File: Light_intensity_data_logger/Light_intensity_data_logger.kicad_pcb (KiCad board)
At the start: 2 copper layers, 105 x 69 mm, 27 parts, among them J1 Wire_to_Vbat, Q1 NTJD4001NT1G, Q2 NTJD4001NT1G, U1 BME280, U2 TCS34725FN, U3 TSL25911FN, U4 Teensy3.6

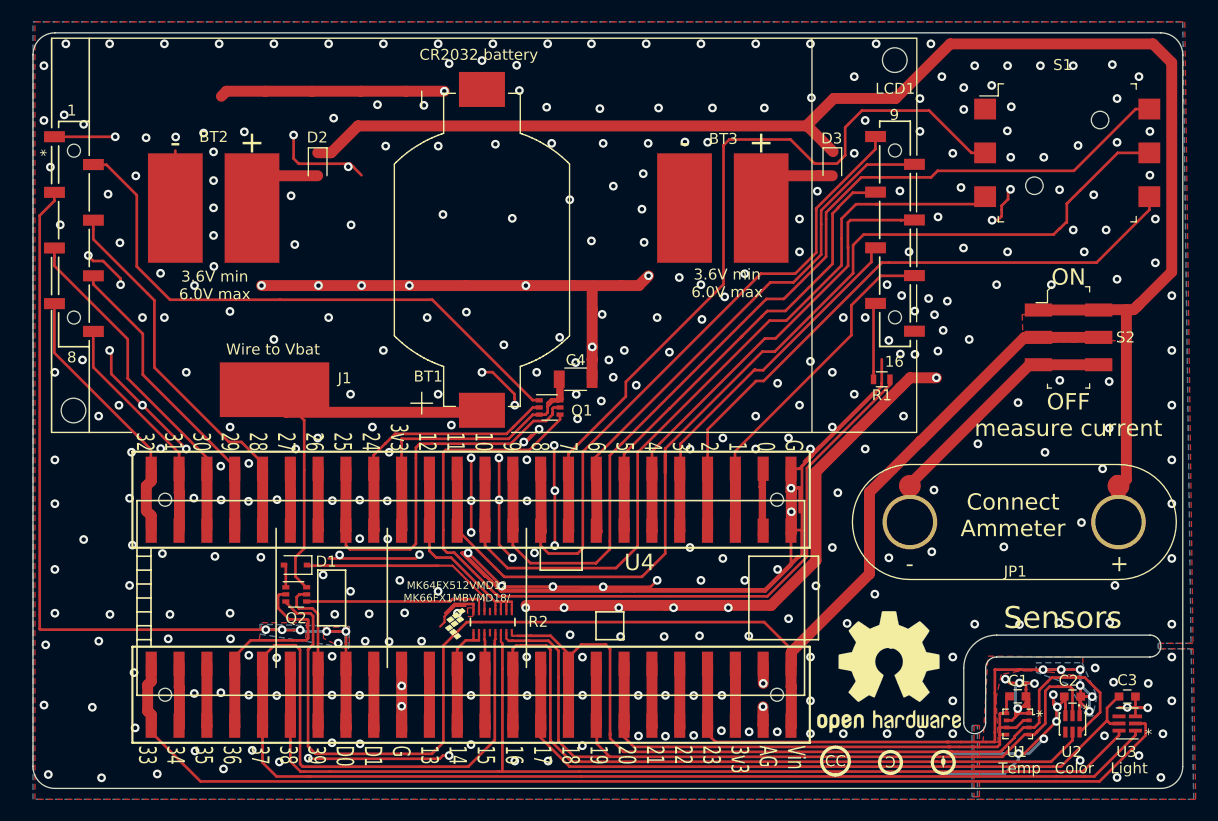
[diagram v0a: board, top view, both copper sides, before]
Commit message: Parts numbered in order, courtyards fixed, bigger banana pads
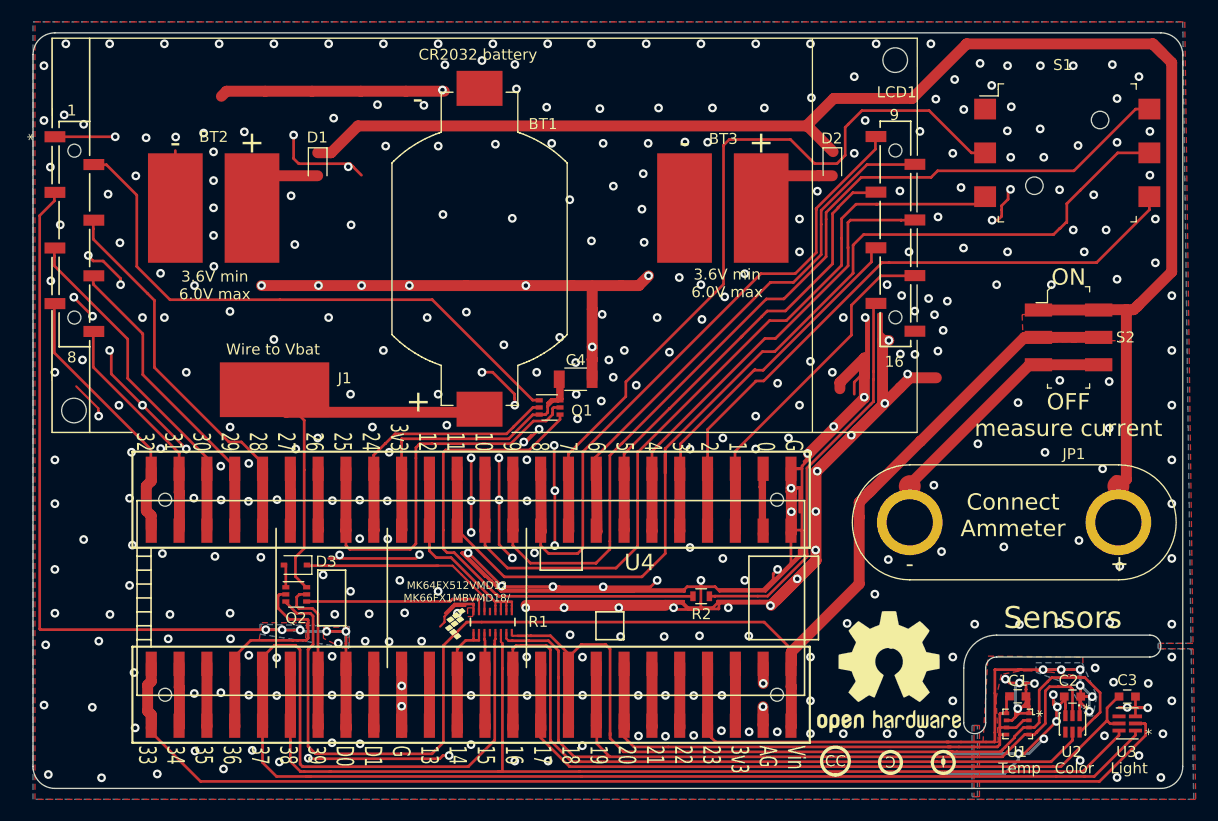
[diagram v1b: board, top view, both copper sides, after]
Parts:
- moved R2 25.8 mm to (134.0, 83.5), turned to 0 degrees
- moved BT1 0.24 mm to (113.8, 51.7)
- renumbered D2 to D1, D3 to D2, D1 to D3, R2 to R1, R1 to R2
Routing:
- net GND: track 428.5 -> 508.5 mm, vias 392 -> 395
- net Net-(Q1-Pad4): track 77.2 -> 45.8 mm
- net Net-(LCD1-Pad15): track 7.03 -> 36.4 mm
- net Net-(D1-Pad1): track 146.3 -> 147.5 mm

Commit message: Rewire LED gate to PWM channel
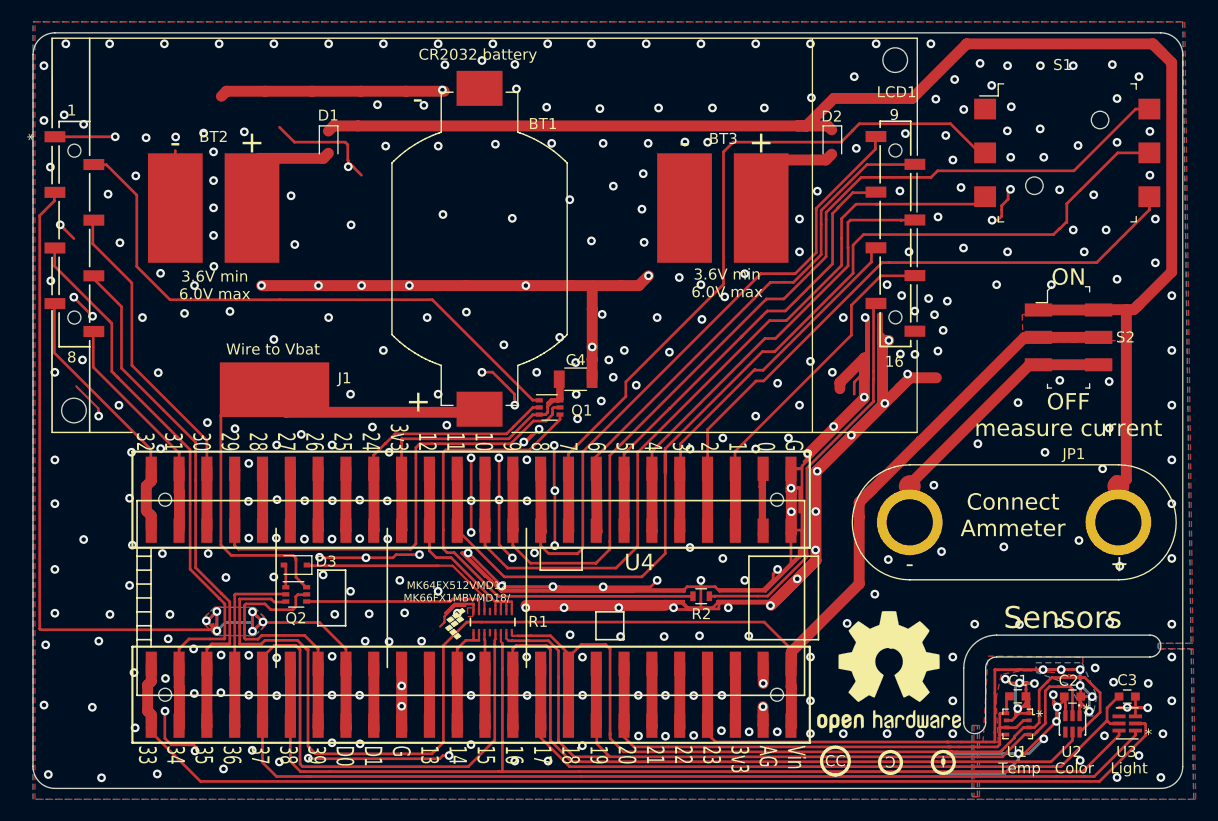
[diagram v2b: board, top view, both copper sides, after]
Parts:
- moved D1 2.24 mm to (100.0, 42.0)
- moved D2 2.00 mm to (146.0, 42.0)
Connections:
- net /17 renamed /Light_Vcc
- net /20 renamed /Temp_Vcc
- net /23 renamed /Color_Vcc
- net /24 renamed /LCD_toggle
- net /36 renamed /Coin_test
- net /39 renamed /Bat_test
- net /DAC0 renamed /LCD_contrast
- Q1 pad 5: /25 -> /LED_PWM
- U4 pad 17: /25 -> Net-(U4-Pad17)
- U4 pad 20: /RS -> Net-(U4-Pad20)
- U4 pad 21: /E -> /LED_PWM
- U4 pad 22: /RW -> /RS
- U4 pad 31: Net-(U4-Pad31) -> /RW
- U4 pad 32: Net-(U4-Pad32) -> /E
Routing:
- net /LED_PWM: track 0.00 -> 47.8 mm
- net /25: track 37.6 -> 0.00 mm
- net /RW: track 31.7 -> 54.0 mm
- net /E: track 28.5 -> 48.4 mm
- net /Bat_test: track 15.1 -> 25.9 mm
- net /LCD_contrast: track 84.1 -> 93.9 mm
- net /Vin: track 123.6 -> 132.4 mm
- net Net-(BT1-Pad+): track 41.5 -> 50.2 mm
- net Net-(U4-Pad20): track 0.00 -> 6.26 mm
- net GND: track 508.5 -> 502.2 mm, vias 395 -> 396
- net Net-(U4-Pad32): track 5.90 -> 0.00 mm
- net Net-(U4-Pad31): track 5.80 -> 0.00 mm
- net Net-(U4-Pad17): track 0.00 -> 5.71 mm
- net Net-(BT2-Pad1): track 6.43 -> 12.0 mm
- net /7*: track 71.4 -> 66.5 mm
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
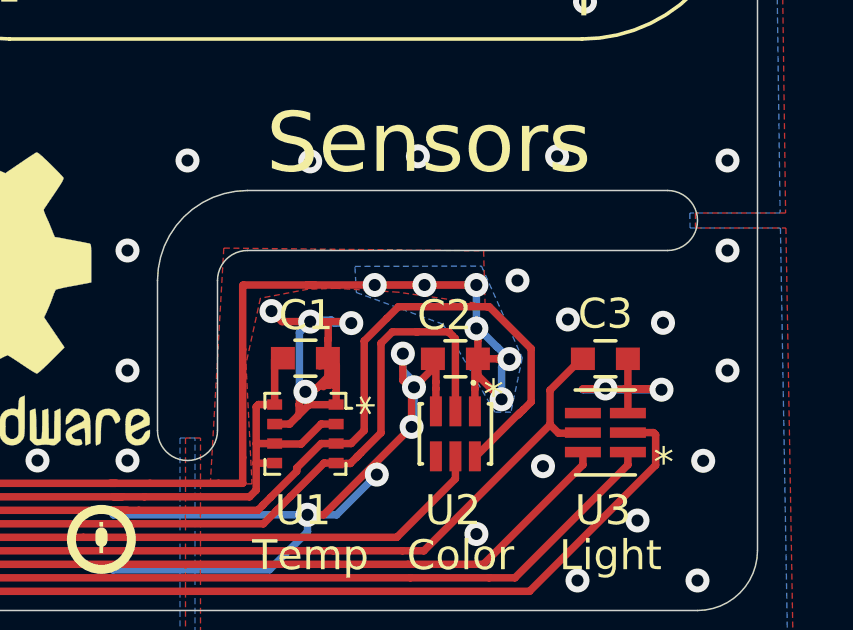
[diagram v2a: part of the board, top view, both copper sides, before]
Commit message: Switch to 1uF caps for sensors per light sensor spec sheet
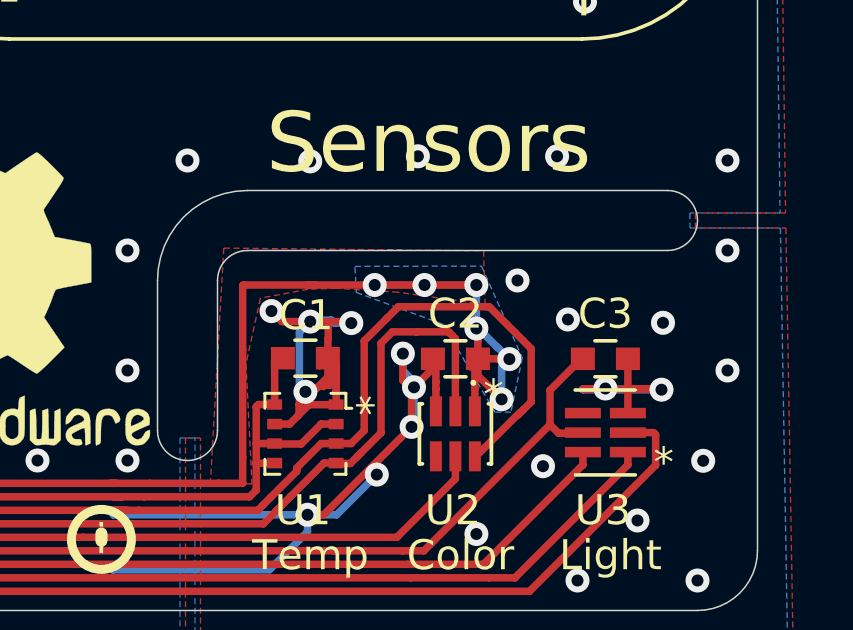
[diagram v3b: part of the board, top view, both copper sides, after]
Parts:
- C1, C2, C3: value 0.1uF -> 1uF
